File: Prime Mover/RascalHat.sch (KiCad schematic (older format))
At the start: 26 parts, among them J10 Conn_01x04_Male, J11 Conn_01x03_Male, J12 Conn_01x03_Male, J13 Conn_01x07_Male, J17 Conn_01x02_Male, J2 Conn_01x09_Male, J4 Conn_01x04_Male, J5 Conn_01x07_Male

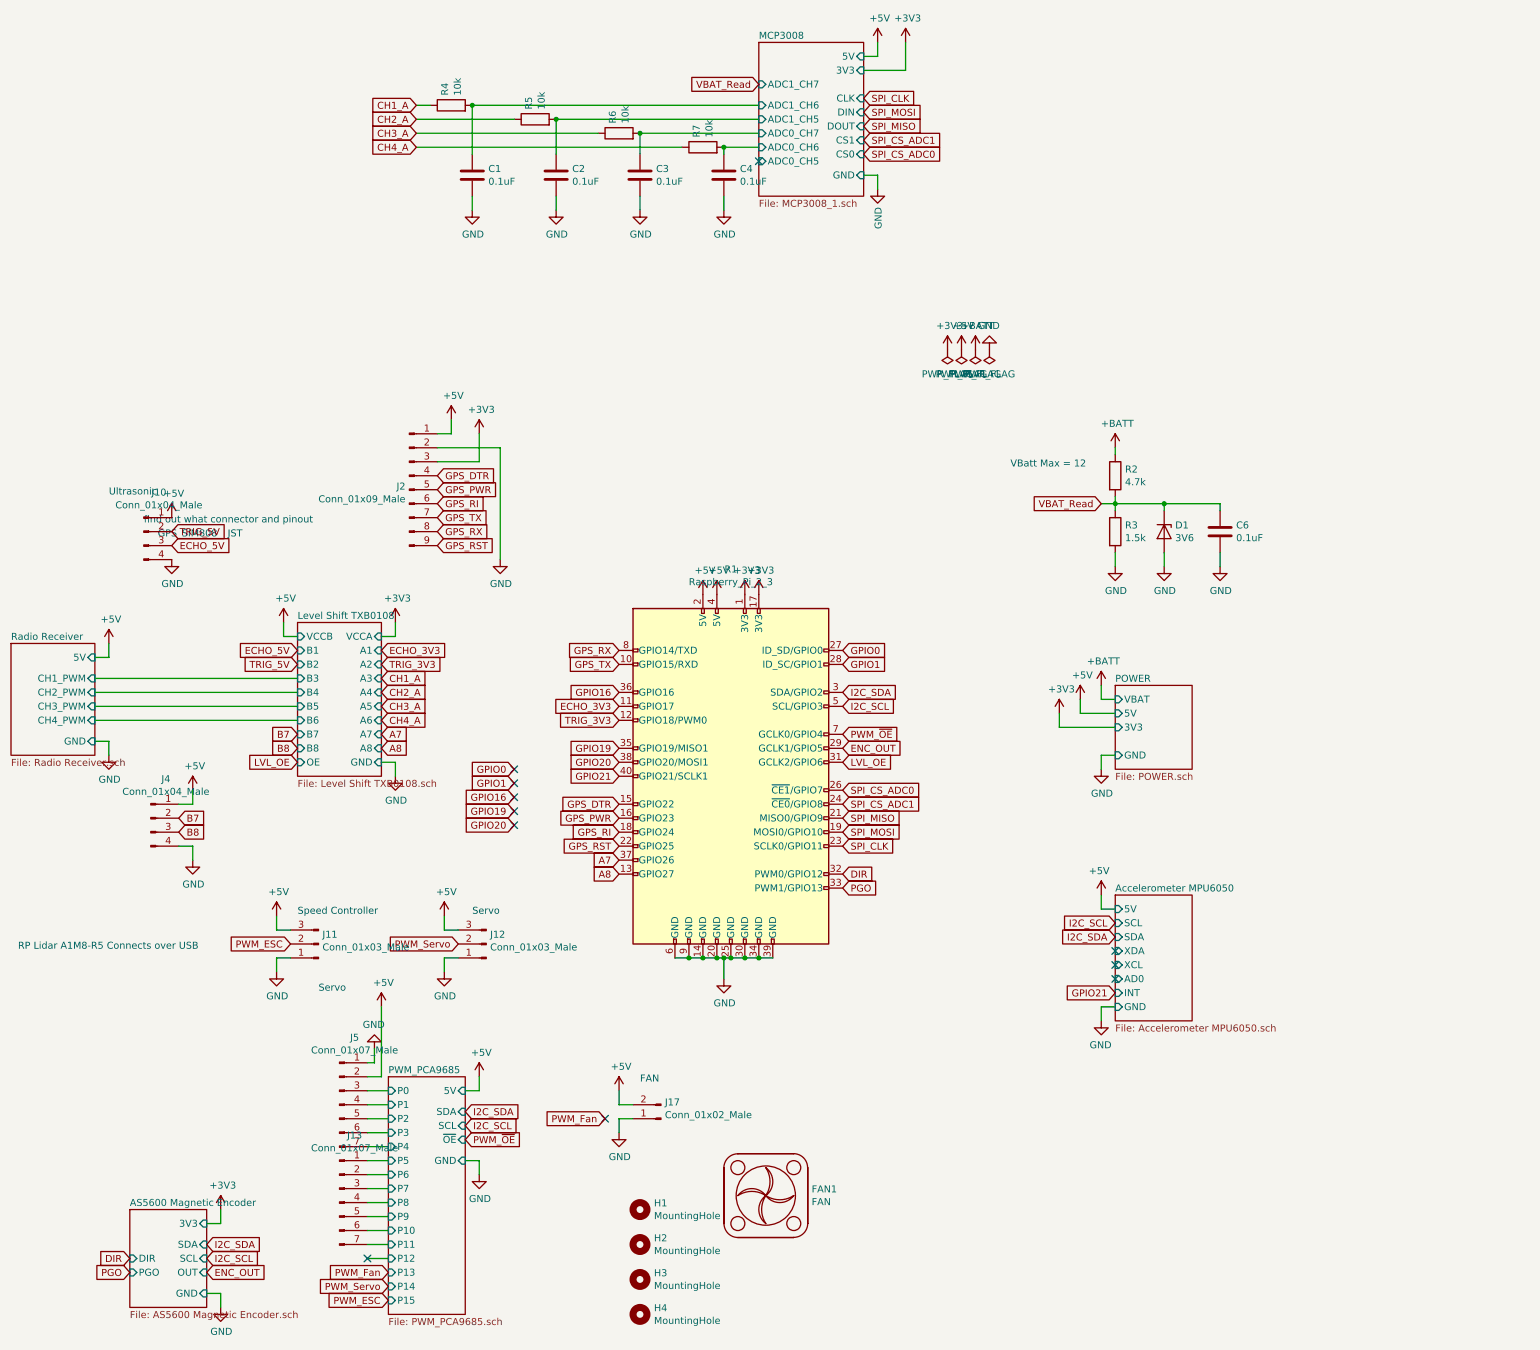
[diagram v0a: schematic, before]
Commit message: schematic capacitors added, pcb done, gerbers generated
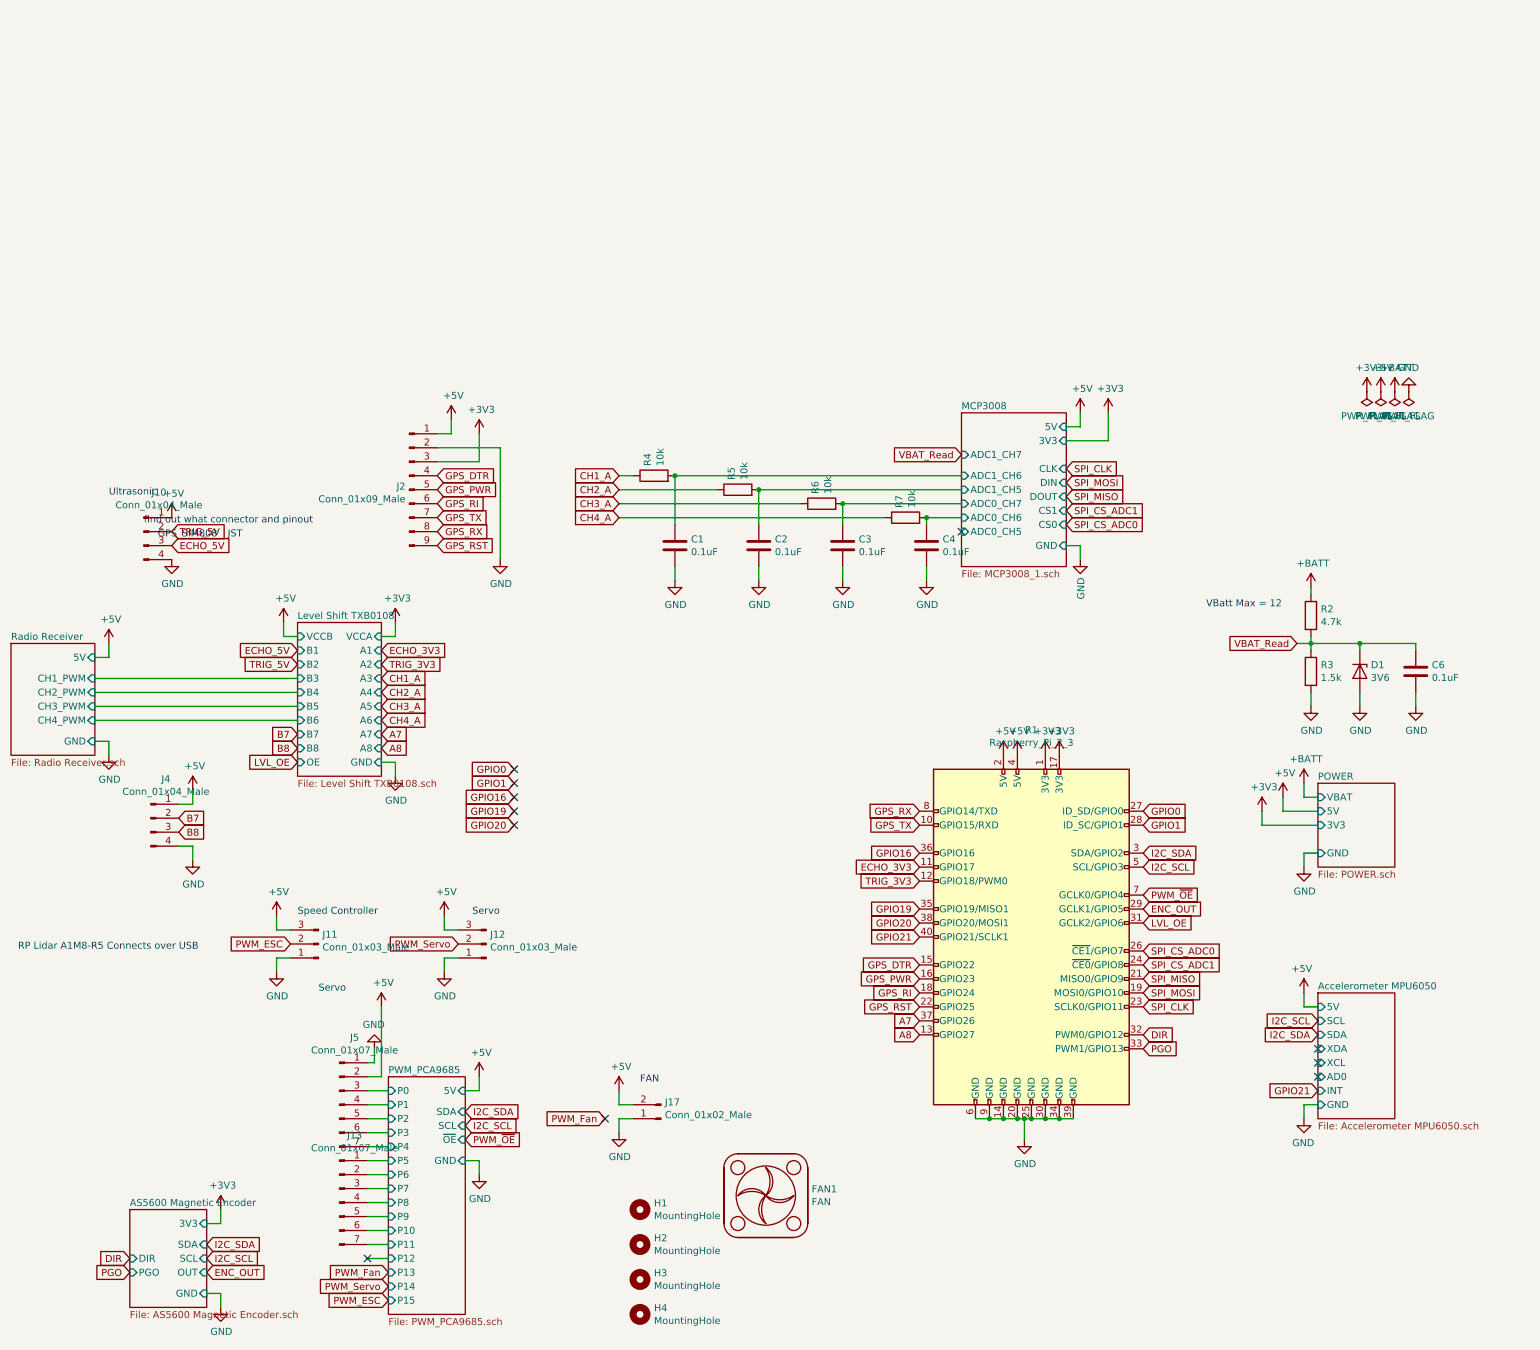
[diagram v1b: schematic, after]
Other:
- moved on the sheet: C1, C2, C3, C4, C6, D1, R1, R2, R3, R4, R5, R6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

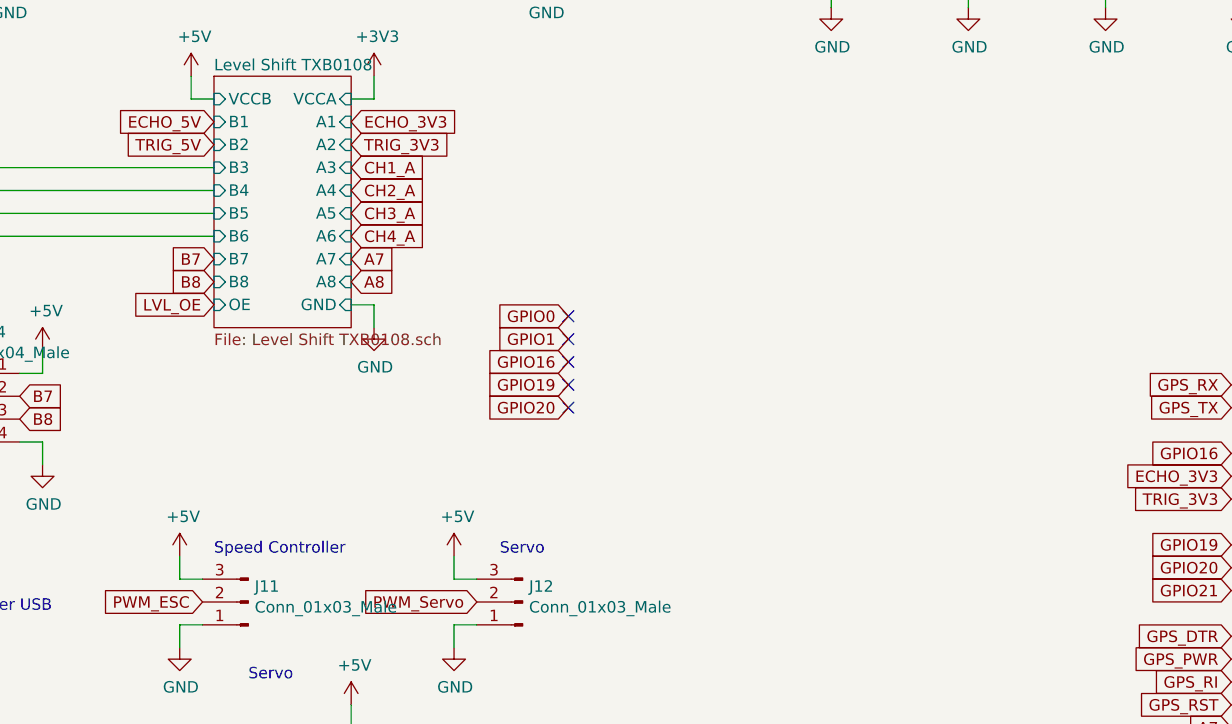
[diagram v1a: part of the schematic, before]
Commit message: pcb XT60 location adjusted, i2C pullup resistors added
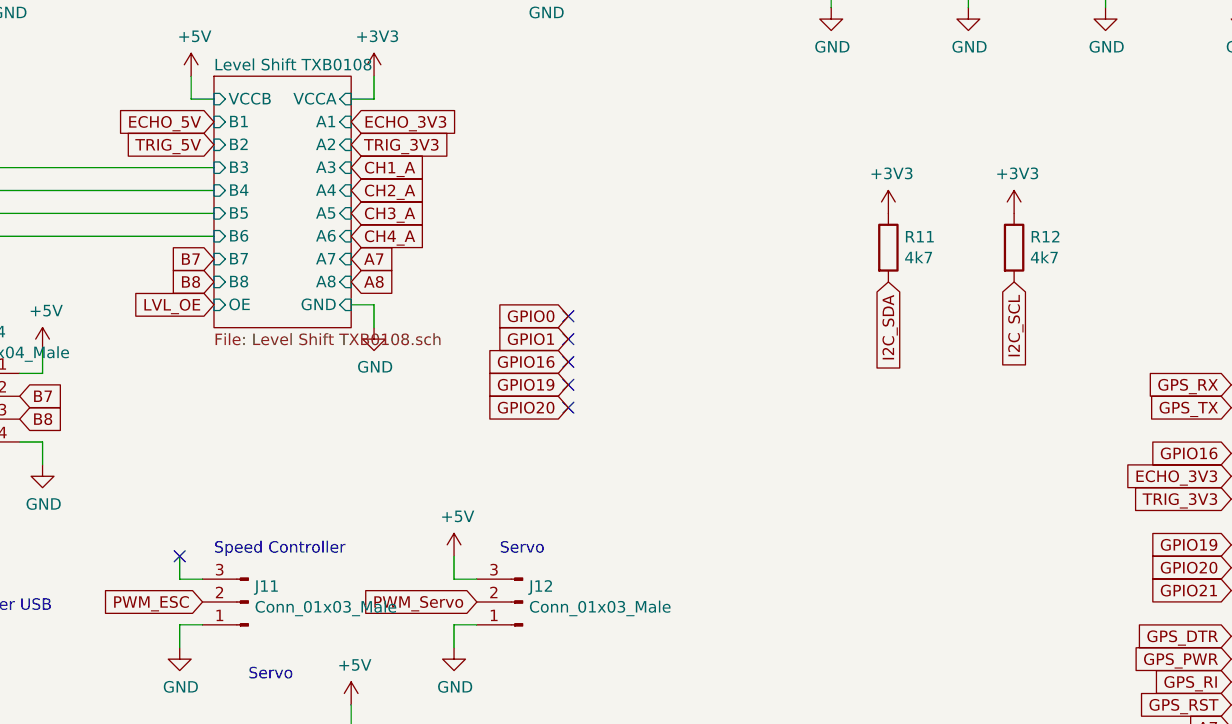
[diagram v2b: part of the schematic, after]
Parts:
- added R11, R12: 4k7, Resistor_SMD:R_0805_2012Metric, symbol Device:R
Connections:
- net +3V3: now also R11.1, R12.1
- net +5V: no longer J11.3 (Pin_3)
- net I2C_SCL: now also R12.2
- net I2C_SDA: now also R11.2
- no-connect marks 11 -> 12
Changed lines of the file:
@@
-$EndComp
-$Comp
-L power:+5V #PWR01
-U 1 1 6148541B
-P 2450 4750
-F 0 "#PWR01" H 2450 4600 50  0001 C CNN
-F 1 "+5V" H 2465 4923 50  0000 C CNN
-F 2 "" H 2450 4750 50  0001 C CNN
-F 3 "" H 2450 4750 50  0001 C CNN
-	1    2450 4750
-	1    0    0    -1
 $EndComp
 $Comp
@@
 NoConn ~ 4150 4000
 NoConn ~ 4150 4100
+NoConn ~ 2450 4750
+$Comp
+L Device:R R11
+U 1 1 61877A47
+P 5550 3400
+F 0 "R11" H 5620 3446 50  0000 L CNN
+F 1 "4k7" H 5620 3355 50  0000 L CNN
+F 2 "Resistor_SMD:R_0805_2012Metric" V 5480 3400 50  0001 C CNN
+F 3 "~" H 5550 3400 50  0001 C CNN
+	1    5550 3400
+	1    0    0    -1
+$EndComp
+Text GLabel 6100 3550 3    50   Input ~ 0
+I2C_SCL
+Text GLabel 5550 3550 3    50   Input ~ 0
+I2C_SDA
+$Comp
+L Device:R R12
+U 1 1 618872A0
+P 6100 3400
+F 0 "R12" H 6170 3446 50  0000 L CNN
+F 1 "4k7" H 6170 3355 50  0000 L CNN
+F 2 "Resistor_SMD:R_0805_2012Metric" V 6030 3400 50  0001 C CNN
+F 3 "~" H 6100 3400 50  0001 C CNN
+	1    6100 3400
+	1    0    0    -1
+$EndComp
+$Comp
+L power:+3V3 #PWR0118
+U 1 1 6188D984
+P 5550 3250
+F 0 "#PWR0118" H 5550 3100 50  0001 C CNN
+F 1 "+3V3" H 5565 3423 50  0000 C CNN
+F 2 "" H 5550 3250 50  0001 C CNN
+F 3 "" H 5550 3250 50  0001 C CNN
+	1    5550 3250
+	1    0    0    -1
+$EndComp
+$Comp
+L power:+3V3 #PWR0119
+U 1 1 6188E419
+P 6100 3250
+F 0 "#PWR0119" H 6100 3100 50  0001 C CNN
+F 1 "+3V3" H 6115 3423 50  0000 C CNN
+F 2 "" H 6100 3250 50  0001 C CNN
+F 3 "" H 6100 3250 50  0001 C CNN
+	1    6100 3250
+	1    0    0    -1
+$EndComp
 $EndSCHEMATC
